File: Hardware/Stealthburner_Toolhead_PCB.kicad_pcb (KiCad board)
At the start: 4 copper layers, 47 x 40 mm, 124 parts, among them J1 Conn_01x02, J10 Conn_01x05, J11 Conn_01x04, J12 Conn_01x04, J2 Conn_01x03, J3 TestPoint, J4 Conn_01x02, J5 Conn_01x03, J6 Conn_01x02, J7 Conn_01x05, J8 Conn_01x03, J9 Conn_01x02, Q1 AO3400A, Q2 AO3400A, Q3 WSD4038DN, U1 BL9342, U10 74LVC1G32, U11 TMC2209-LA-T, U12 MAX31865xTP, U13 ADXL343, U2 ME6209A50M3G, U3 ME6209A33M3G, U4 W25Q16JVUXIQ, U5 USBLC6-2SC6, U6 74LVC2G17, U7 RP2040, U8 74LVC2G17, U9 SHT20, Y1 CSTNE12M0

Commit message: 1
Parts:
- added C35: 100nF/1uF, Capacitor_SMD:C_0603_1608Metric, B.Cu at (120.8, 119.0)
- added kibuzzard-62BB2226: G***, kibuzzard-62BB2226, B.Cu at (126.3, 99.1)
- added kibuzzard-62BB2232: G***, kibuzzard-62BB2232, B.Cu at (121.4, 98.2)
- added kibuzzard-62BB2232: G***, kibuzzard-62BB2232, B.Cu at (121.5, 102.2)
- added kibuzzard-62BB2232: G***, kibuzzard-62BB2232, B.Cu at (126.3, 102.0)
- added kibuzzard-62BD8821: G***, kibuzzard-62BD8821, B.Cu at (119.2, 102.2)
- added kibuzzard-62BD8832: G***, kibuzzard-62BD8832, B.Cu at (119.2, 98.2)
- added kibuzzard-62BD8846: G***, kibuzzard-62BD8846, B.Cu at (126.4, 100.5)
- added kibuzzard-62BD8A50: G***, kibuzzard-62BD8A50, B.Cu at (109.8, 110.5)
- added kibuzzard-62BD8A57: G***, kibuzzard-62BD8A57, B.Cu at (109.8, 112.5)
- added kibuzzard-62BD8A5A: G***, kibuzzard-62BD8A5A, B.Cu at (109.8, 114.5)
- added kibuzzard-62BD8A5E: G***, kibuzzard-62BD8A5E, B.Cu at (109.8, 116.4)
- added kibuzzard-62BD8C64: G***, kibuzzard-62BD8C64, B.Cu at (113.9, 118.6)
- added kibuzzard-62BD8C8D: G***, kibuzzard-62BD8C8D, B.Cu at (114.7, 101.1)
- moved C23 1.68 mm to (106.4, 109.4), turned to 90 degrees
- moved JP3 0.51 mm to (123.3, 119.0)
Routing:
- net /RTDIN-: track 3.40 -> 5.70 mm
- net /RTDIN+: track 3.20 -> 4.88 mm
- net /FORCE+: track 4.66 -> 5.18 mm
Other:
- board text added: "DET1"
- board text added: "DET2"
- board text added: "PPWM"
- board text added: "PWM1"
- board text added: "PWM2"
- board text added: "SPWM"
- board text added: "VCC"
- board text removed: "12V"
- board text removed: "24V P25 GND"
- board text removed: "GND P36"
- board text removed: "GND P41"
- board text removed: "PWM"

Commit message: 1
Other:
- board text added: "Designed by"
- board text added: "JLCJLCJLC"
- board text added: "V1.0"

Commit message: 1
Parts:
- added R22: 10K, Resistor_SMD:R_0402_1005Metric, B.Cu at (129.7, 110.7)
- added R23: 10K, Resistor_SMD:R_0402_1005Metric, B.Cu at (129.7, 111.7)
- C1: value 22uF -> 22uF/35V
- L1: value 15uH -> 6.2uH
- renumbered C26 to C27, C27 to C28, C28 to C29, C29 to C30, C30 to C31, C31 to C32, C32 to C33, C33 to C34, C34 to C35, C35 to C36, R21 to R24, R22 to R25, R23 to R26, R24 to R27, R25 to R28, R26 to R29, R27 to R30, R28 to R31, U10 to U11, U11 to U12, U12 to U13, U13 to U14
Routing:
- net +3V3: track 192.1 -> 196.6 mm
- net /IIC0_SDA: track 28.9 -> 30.5 mm
- net /IIC0_SCL: track 27.4 -> 28.3 mm
- net GND: vias 125 -> 126

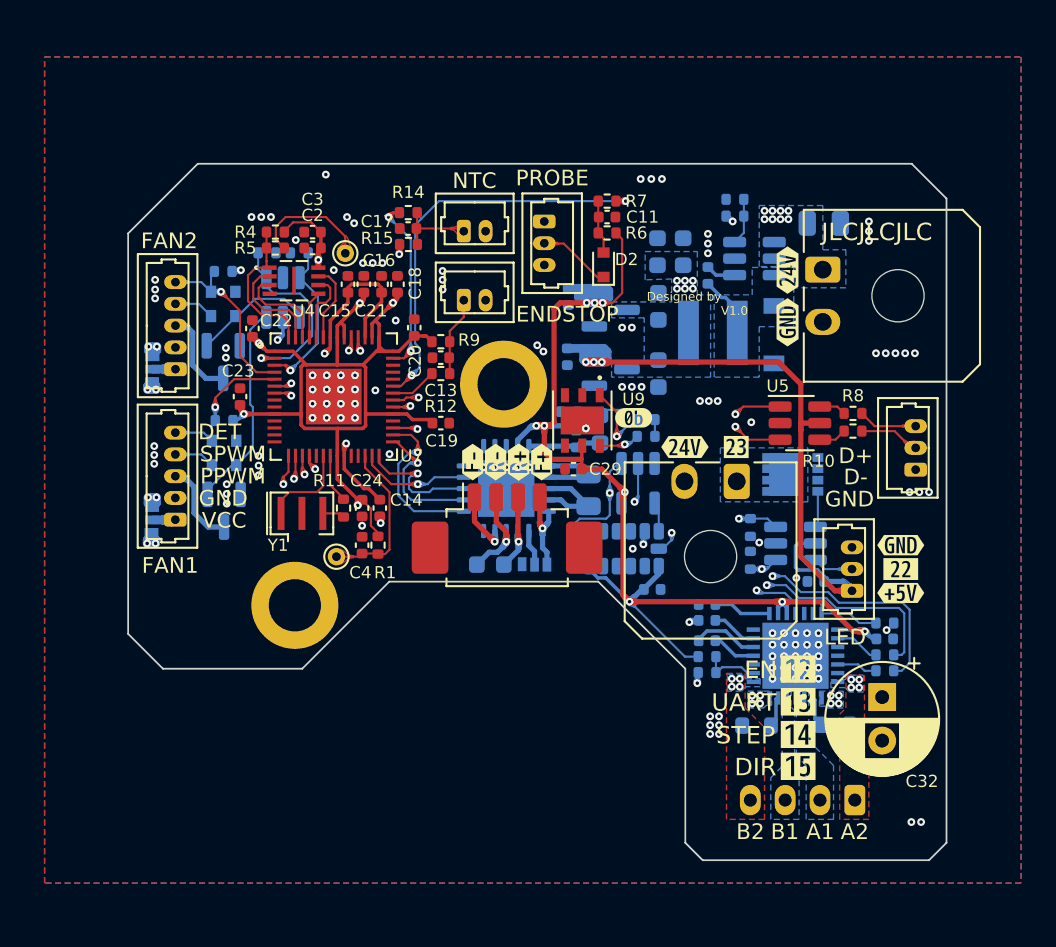
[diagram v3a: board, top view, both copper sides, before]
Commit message: V1.1 Release
* Add a TVS for TMC2209
* Replaced SHT21 with Si7021
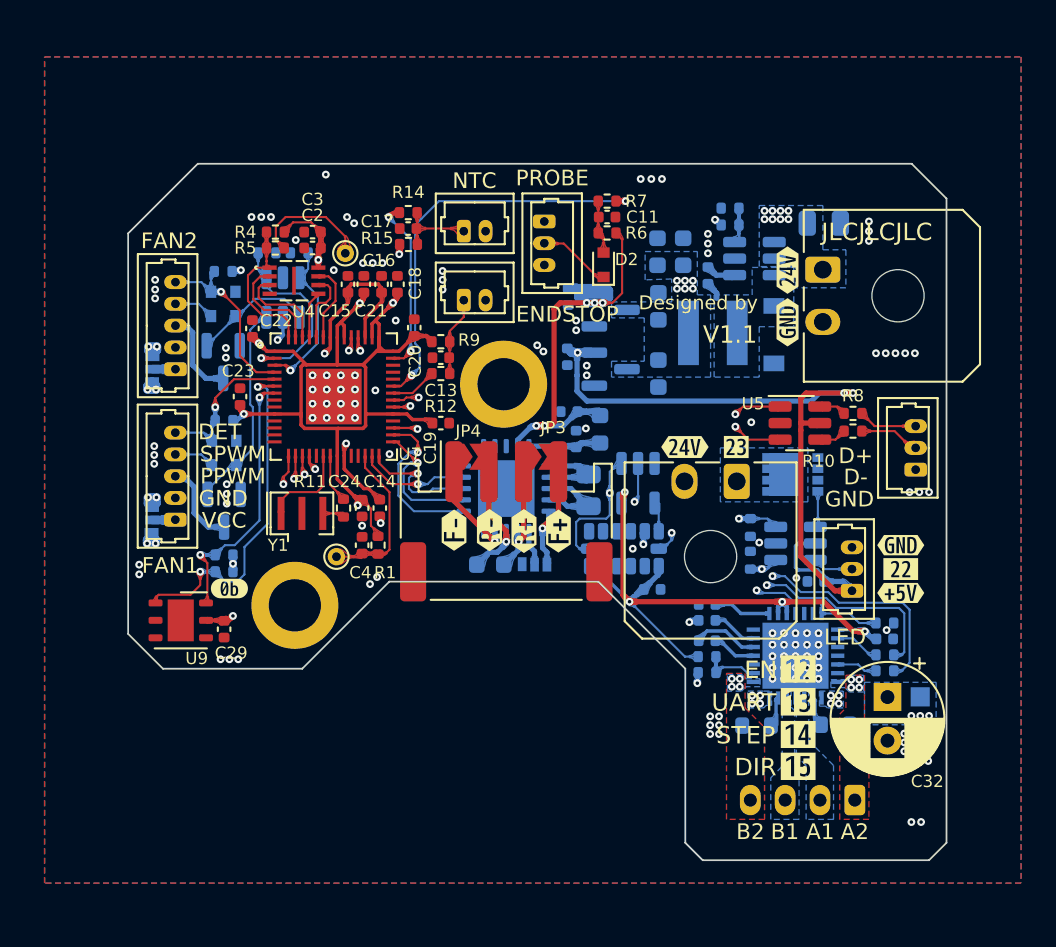
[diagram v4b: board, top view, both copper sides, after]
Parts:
- removed kibuzzard-62BB238A: G***, kibuzzard-62BB238A
- removed kibuzzard-62BB238F: G***, kibuzzard-62BB238F
- removed kibuzzard-62BB2393: G***, kibuzzard-62BB2393
- removed kibuzzard-62BB2397: G***, kibuzzard-62BB2397
- added D7: SMF28A, Diode_SMD:D_SOD-123F, B.Cu at (145.5, 128.0)
- added G***: LOGO, LOGO, F.Cu at (132.0, 107.0)
- added JP3: SolderJumper_2_Open, 1_Library:SolderJumper-2_P1.3mm_Open_TrianglePad1.0x1.5mm, F.Cu at (123.5, 112.8)
- added JP4: SolderJumper_2_Open, 1_Library:SolderJumper-2_P1.3mm_Open_TrianglePad1.0x1.5mm, F.Cu at (119.5, 112.8)
- added kibuzzard-62E7C936: G***, kibuzzard-62E7C936, F.Cu at (118.7, 117.0)
- added kibuzzard-62E7C93B: G***, kibuzzard-62E7C93B, F.Cu at (120.8, 117.0)
- added kibuzzard-62E7C943: G***, kibuzzard-62E7C943, F.Cu at (122.7, 117.1)
- added kibuzzard-62E7C964: G***, kibuzzard-62E7C964, F.Cu at (124.7, 117.1)
- D1: value CUS10S30 -> SS14L
- J11: footprint Connector_Molex:Molex_PicoBlade_53261-0471_1x04-1MP_P1.25mm_Horizontal -> 1_Library:JST_PH_S4B-PH-SM4-TB_1x04-1MP_P2.00mm_Horizontal
- R2: value 124K -> 309K
- R3: value 8.87K -> 22.1K
- U1: value BL9342 -> LMR54410
- U9: value SHT20 -> Si7021-A20; footprint 1_Library:SHT20 -> Package_DFN_QFN:DFN-6-1EP_3x3mm_P1mm_EP1.5x2.4mm
- moved U9 25.8 mm to (103.0, 122.2), turned to 0 degrees
- moved R22 25.8 mm to (105.5, 119.4)
- moved kibuzzard-62BB1C3A 25.2 mm to (105.8, 120.4)
- moved R23 25.2 mm to (105.5, 118.5)
- moved C29 22.1 mm to (105.5, 122.7), turned to -90 degrees
- moved J11 1.02 mm to (121.7, 116.5)
- moved R3 0.58 mm to (134.6, 98.6)
- moved R2 0.58 mm to (134.6, 99.5)
- moved C32 0.30 mm to (143.6, 126.6)
- renumbered JP3 to JP5
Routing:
- net /IIC0_SCL: track 28.3 -> 15.2 mm
- net /IIC0_SDA: track 30.5 -> 19.6 mm
- net +5V: track 60.5 -> 63.5 mm
- net +3V3: track 196.6 -> 193.8 mm, vias 17 -> 19
- net Net-(C7-Pad1): track 3.65 -> 1.05 mm
- net /FORCE-: track 3.65 -> 5.60 mm
- net /FORCE+: track 5.18 -> 6.96 mm
- net /RTDIN-: track 5.70 -> 7.34 mm
- net /RTDIN+: track 4.88 -> 6.45 mm
- net +12V: track 69.1 -> 68.1 mm
- net Net-(R2-Pad2): track 2.67 -> 2.05 mm
- net GND: vias 126 -> 121
- net +24V: vias 21 -> 24
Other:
- board text added: "V1.1"
- board text removed: "V1.0"
